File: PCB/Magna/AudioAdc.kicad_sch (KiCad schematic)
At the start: 19 parts, among them J301 PSG01550, U301 WM8782SEDS

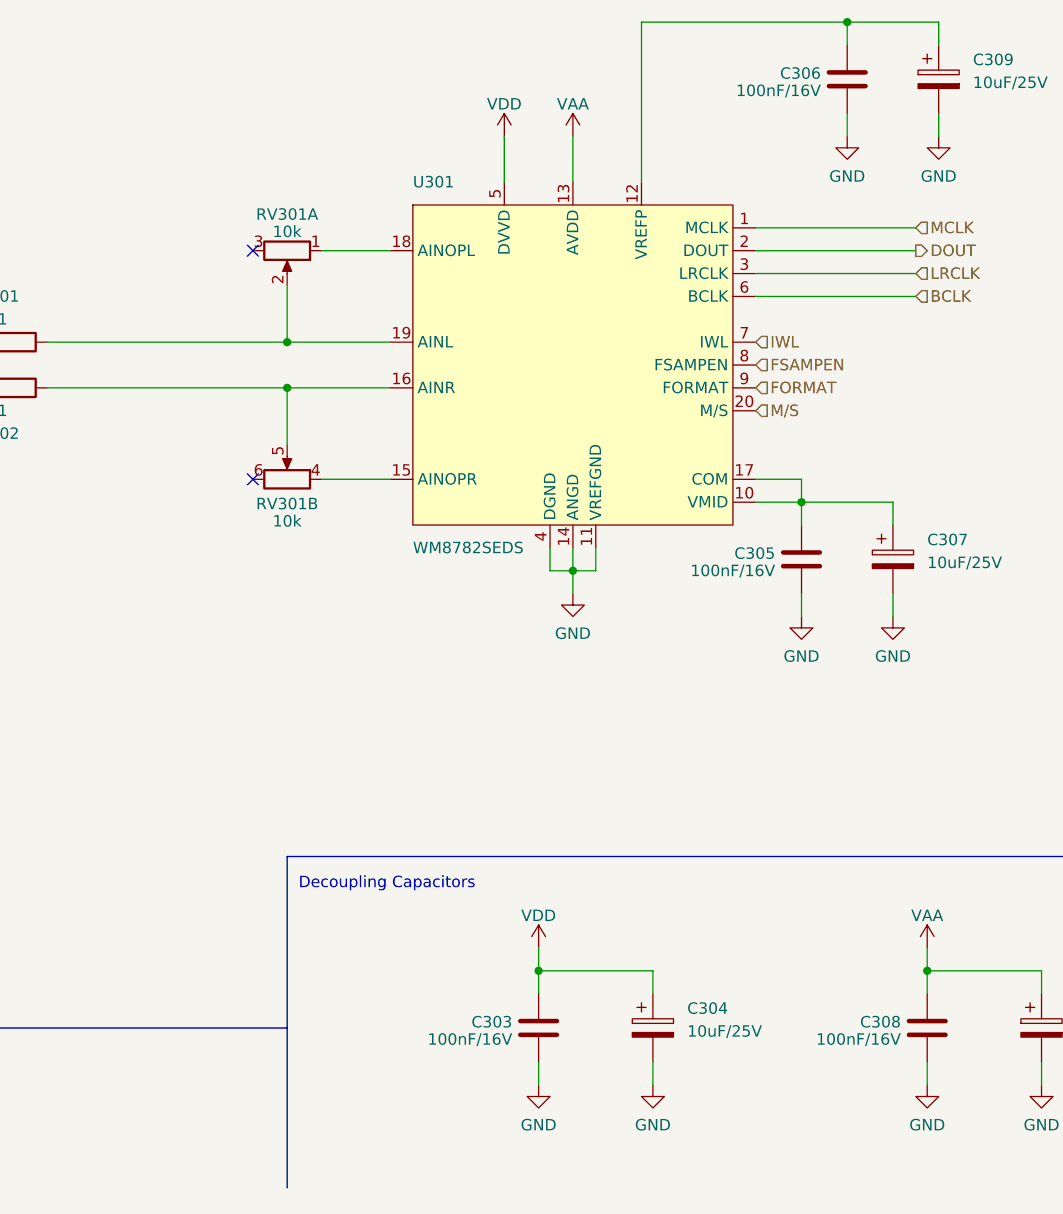
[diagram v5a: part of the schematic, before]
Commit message: Add even more component footprints and partnumbers
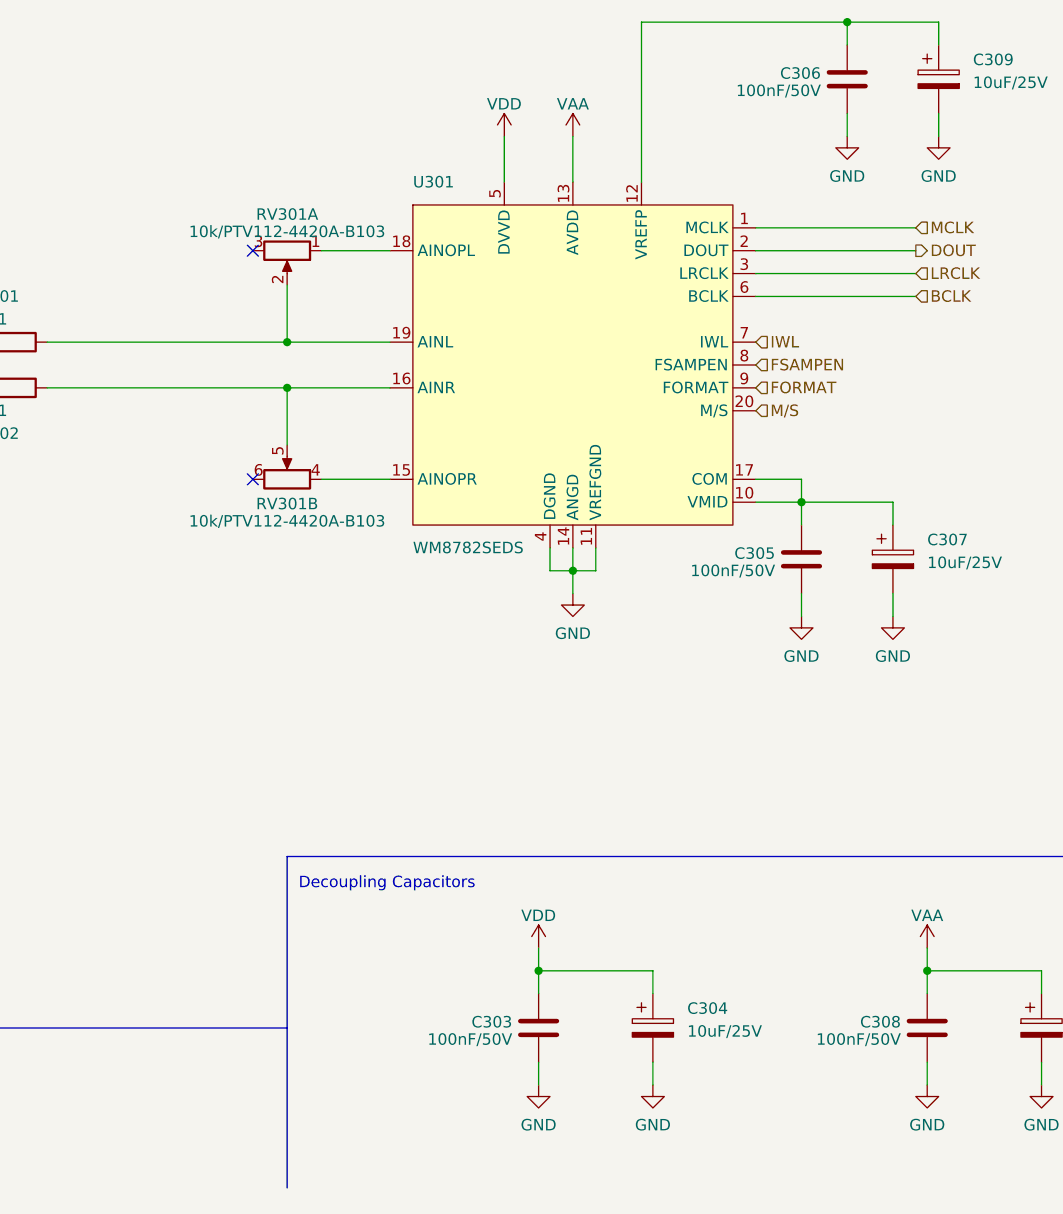
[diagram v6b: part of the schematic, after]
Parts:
- C303, C305, C306, C308: value 100nF/16V -> 100nF/50V; footprint Capacitor_SMD:C_0805_2012Metric -> Capacitor_SMD:C_0805_2012Metric_Pad1.18x1.45mm_HandSolder; LCSC C218638 -> C49678
- J301: footprint (none) -> Skrooter_footprints:psg01550
- R301, R302: footprint Resistor_SMD:R_0805_2012Metric -> Resistor_SMD:R_0805_2012Metric_Pad1.20x1.40mm_HandSolder
- RV301: value 10k -> 10k/PTV112-4420A-B103; footprint (none) -> Skrooter_footprints:Potentiometer_Bourns_PTV09A-1_Dual_Vertical
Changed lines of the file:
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@@
       (effects (font (size 1.27 1.27)) (justify left))
     )
-    (property "Footprint" "Resistor_SMD:R_0805_2012Metric" (at 147.32 72.898 90)
+    (property "Footprint" "Resistor_SMD:R_0805_2012Metric_Pad1.20x1.40mm_HandSolder" (at 147.32 72.898 90)
       (effects (font (size 1.27 1.27)) hide)
     )
@@
       (effects (font (size 1.27 1.27)) (justify left))
     )
-    (property "Value" "100nF/16V" (at 237.109 43.1873 0)
-      (effects (font (size 1.27 1.27)) (justify left))
-    )
-    (property "Footprint" "Capacitor_SMD:C_0805_2012Metric" (at 239.0648 45.72 0)
+    (property "Value" "100nF/50V" (at 237.109 43.1873 0)
+      (effects (font (size 1.27 1.27)) (justify left))
+    )
+    (property "Footprint" "Capacitor_SMD:C_0805_2012Metric_Pad1.18x1.45mm_HandSolder" (at 239.0648 45.72 0)
       (effects (font (size 1.27 1.27)) hide)
     )
@@
       (effects (font (size 1.27 1.27)) hide)
     )
-    (property "LCSC" "C218638" (at 240.03 41.91 0)
+    (property "LCSC" "C49678" (at 240.03 41.91 0)
       (effects (font (size 1.27 1.27)) hide)
     )
@@
       (effects (font (size 1.27 1.27)) (justify left))
     )
-    (property "Value" "100nF/16V" (at 245.999 148.5973 0)
-      (effects (font (size 1.27 1.27)) (justify left))
-    )
-    (property "Footprint" "Capacitor_SMD:C_0805_2012Metric" (at 247.9548 151.13 0)
+    (property "Value" "100nF/50V" (at 245.999 148.5973 0)
+      (effects (font (size 1.27 1.27)) (justify left))
+    )
+    (property "Footprint" "Capacitor_SMD:C_0805_2012Metric_Pad1.18x1.45mm_HandSolder" (at 247.9548 151.13 0)
       (effects (font (size 1.27 1.27)) hide)
     )
@@
       (effects (font (size 1.27 1.27)) hide)
     )
-    (property "LCSC" "C218638" (at 248.92 147.32 0)
+    (property "LCSC" "C49678" (at 248.92 147.32 0)
       (effects (font (size 1.27 1.27)) hide)
     )
@@
       (effects (font (size 1.27 1.27)))
     )
-    (property "Value" "10k" (at 177.8 58.8551 90)
-      (effects (font (size 1.27 1.27)))
-    )
-    (property "Footprint" "" (at 177.8 60.96 0)
+    (property "Value" "10k/PTV112-4420A-B103" (at 177.8 58.8551 90)
+      (effects (font (size 1.27 1.27)))
+    )
+    (property "Footprint" "Skrooter_footprints:Potentiometer_Bourns_PTV09A-1_Dual_Vertical" (at 177.8 60.96 0)
       (effects (font (size 1.27 1.27)) hide)
     )
@@
       (effects (font (size 1.27 1.27)) (justify left))
     )
-    (property "Value" "100nF/16V" (at 232.029 96.5273 0)
-      (effects (font (size 1.27 1.27)) (justify left))
-    )
-    (property "Footprint" "Capacitor_SMD:C_0805_2012Metric" (at 233.9848 99.06 0)
+    (property "Value" "100nF/50V" (at 232.029 96.5273 0)
+      (effects (font (size 1.27 1.27)) (justify left))
+    )
+    (property "Footprint" "Capacitor_SMD:C_0805_2012Metric_Pad1.18x1.45mm_HandSolder" (at 233.9848 99.06 0)
       (effects (font (size 1.27 1.27)) hide)
     )
@@
       (effects (font (size 1.27 1.27)) hide)
     )
-    (property "LCSC" "C218638" (at 234.95 95.25 0)
+    (property "LCSC" "C49678" (at 234.95 95.25 0)
       (effects (font (size 1.27 1.27)) hide)
     )
@@
       (effects (font (size 1.27 1.27)))
     )
-    (property "Footprint" "" (at 110.49 76.2 0)
+    (property "Footprint" "Skrooter_footprints:psg01550" (at 110.49 76.2 0)
       (effects (font (size 1.27 1.27)) hide)
     )
@@
       (effects (font (size 1.27 1.27)) (justify left))
     )
-    (property "Value" "100nF/16V" (at 202.819 148.5973 0)
-      (effects (font (size 1.27 1.27)) (justify left))
-    )
-    (property "Footprint" "Capacitor_SMD:C_0805_2012Metric" (at 204.7748 151.13 0)
+    (property "Value" "100nF/50V" (at 202.819 148.5973 0)
+      (effects (font (size 1.27 1.27)) (justify left))
+    )
+    (property "Footprint" "Capacitor_SMD:C_0805_2012Metric_Pad1.18x1.45mm_HandSolder" (at 204.7748 151.13 0)
       (effects (font (size 1.27 1.27)) hide)
     )
@@
       (effects (font (size 1.27 1.27)) hide)
     )
-    (property "LCSC" "C218638" (at 205.74 147.32 0)
+    (property "LCSC" "C49678" (at 205.74 147.32 0)
       (effects (font (size 1.27 1.27)) hide)
     )
@@
       (effects (font (size 1.27 1.27)))
     )
-    (property "Value" "10k" (at 177.8 91.0195 90)
-      (effects (font (size 1.27 1.27)))
-    )
-    (property "Footprint" "" (at 177.8 86.36 0)
+    (property "Value" "10k/PTV112-4420A-B103" (at 177.8 91.0195 90)
+      (effects (font (size 1.27 1.27)))
+    )
+    (property "Footprint" "Skrooter_footprints:Potentiometer_Bourns_PTV09A-1_Dual_Vertical" (at 177.8 86.36 0)
       (effects (font (size 1.27 1.27)) hide)
     )
@@
       (effects (font (size 1.27 1.27)) (justify left))
     )
-    (property "Footprint" "Resistor_SMD:R_0805_2012Metric" (at 147.32 74.422 90)
-      (effects (font (size 1.27 1.27)) hide)
-    )
+    (property "Footprint" "Resistor_SMD:R_0805_2012Metric_Pad1.20x1.40mm_HandSolder" (at 147.32 74.422 90)
+      (effects (font (size 1.27 1.27)) hide)
+    )
